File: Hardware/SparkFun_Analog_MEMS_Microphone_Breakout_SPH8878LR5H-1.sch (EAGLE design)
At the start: 18 parts, among them U1 OPA344, U3 SPH8878LR5H-1

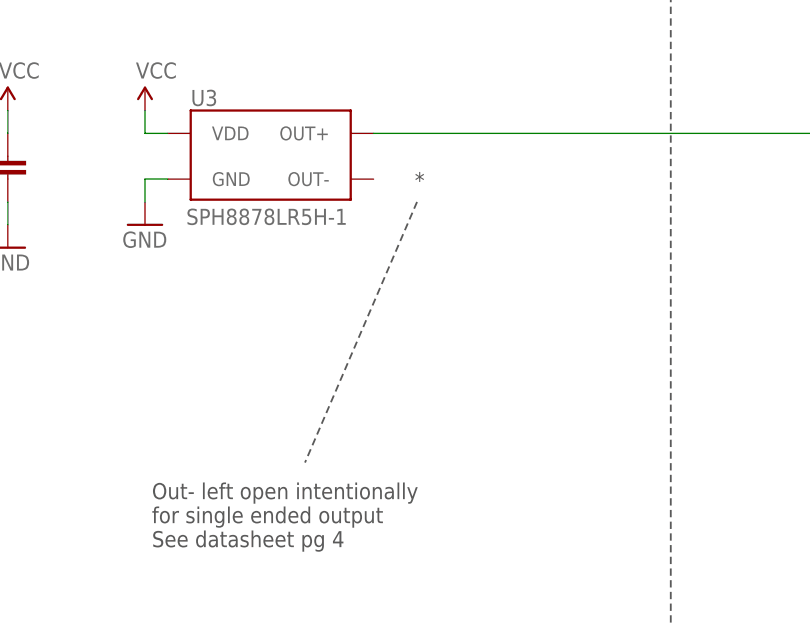
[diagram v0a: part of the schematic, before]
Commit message: Added test point for OUT-
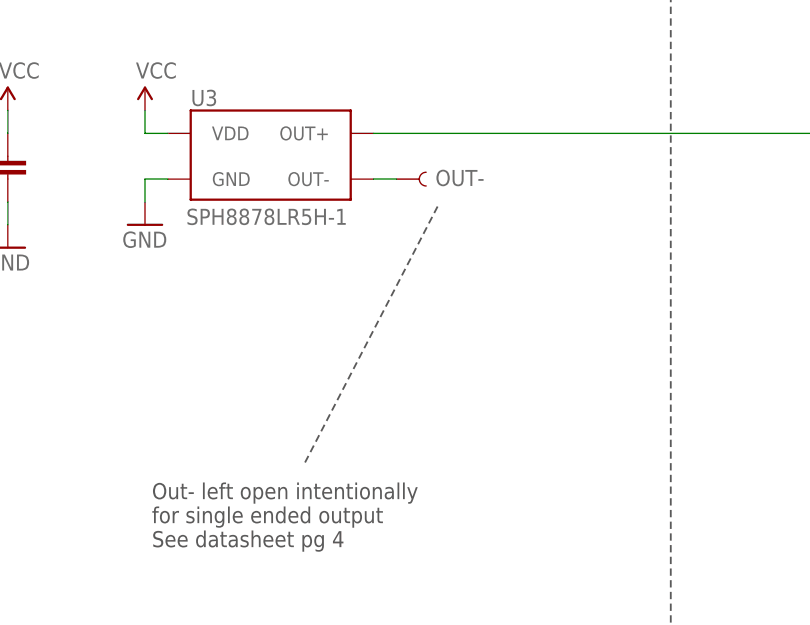
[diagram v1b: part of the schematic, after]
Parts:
- added OUT-: TEST-POINTTP_15TH_THRU, SparkFun-Connectors:TEST-POINTTP_15TH_THRU
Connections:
- new net N$3: OUT-.1, U3.OUT-
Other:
- note removed: "*"
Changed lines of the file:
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@@
 <layer number="56" name="wert" color="7" fill="1" visible="no" active="no"/>
 <layer number="57" name="tCAD" color="7" fill="1" visible="no" active="no"/>
+<layer number="58" name="bCAD" color="7" fill="1" visible="no" active="no"/>
 <layer number="59" name="tCarbon" color="7" fill="1" visible="no" active="no"/>
 <layer number="60" name="bCarbon" color="7" fill="1" visible="no" active="no"/>
@@
 <layer number="250" name="Descript" color="3" fill="1" visible="no" active="no"/>
 <layer number="251" name="SMDround" color="12" fill="11" visible="no" active="no"/>
+<layer number="253" name="Extra" color="7" fill="1" visible="no" active="no"/>
 <layer number="254" name="cooling" color="7" fill="1" visible="yes" active="yes"/>
 <layer number="255" name="routoute" color="7" fill="1" visible="no" active="no"/>
@@
 <part name="FD4" library="SparkFun-Aesthetics" deviceset="FIDUCIAL" device="UFIDUCIAL"/>
 <part name="U3" library="temp" deviceset="SPH8878LR5H-1" device=""/>
+<part name="OUT-" library="SparkFun-Connectors" deviceset="TEST-POINT" device="TP_15TH_THRU" value=""/>
 </parts>
 <sheets>
@@
 for single ended output
 See datasheet pg 4</text>
-<wire x1="78.486" y1="114.3" x2="66.04" y2="85.344" width="0.2032" layer="97" style="shortdash"/>
-<text x="78.232" y="115.824" size="1.778" layer="97" font="vector">*</text>
+<wire x1="80.772" y1="113.792" x2="66.04" y2="85.344" width="0.2032" layer="97" style="shortdash"/>
 </plain>
 <instances>
@@
 <attribute name="NAME" x="53.34" y="124.968" size="1.778" layer="95" font="vector"/>
 <attribute name="VALUE" x="52.832" y="113.538" size="1.778" layer="96" font="vector" align="top-left"/>
+</instance>
+<instance part="OUT-" gate="G$1" x="76.2" y="116.84" smashed="yes">
+<attribute name="NAME" x="80.518" y="116.078" size="1.778" layer="95" font="vector"/>
+<attribute name="VALUE" x="73.66" y="114.3" size="1.778" layer="96" font="vector"/>
 </instance>
 </instances>
@@
 </segment>
 </net>
+<net name="N$3" class="0">
+<segment>
+<pinref part="U3" gate="G$1" pin="OUT-"/>
+<pinref part="OUT-" gate="G$1" pin="1"/>
+<wire x1="76.2" y1="116.84" x2="73.66" y2="116.84" width="0.1524" layer="91"/>
+</segment>
+</net>

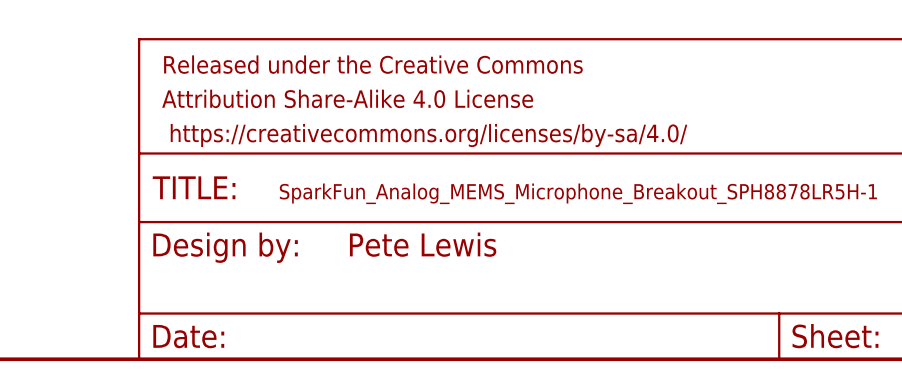
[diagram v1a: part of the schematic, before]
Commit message: Checklist catches
-Attribution for original design
-test point for OUT- moved to 50 though grid
-nudges some vias to avoid silk
-adjust value text objects for assembly sheet
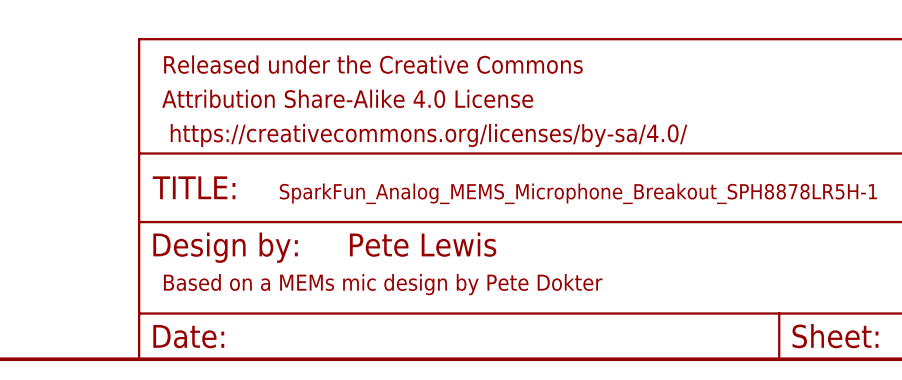
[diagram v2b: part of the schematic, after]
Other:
- note added: "Based on a MEMs mic design by Pete Dokter"
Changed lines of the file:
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@@
 See datasheet pg 4</text>
 <wire x1="80.772" y1="113.792" x2="66.04" y2="85.344" width="0.2032" layer="97" style="shortdash"/>
+<text x="149.86" y="7.62" size="1.778" layer="94" font="vector">Based on a MEMs mic design by Pete Dokter</text>
 </plain>
 <instances>
